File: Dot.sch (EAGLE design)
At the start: 42 parts, among them IC1 CAT24M010TS, IC2 SI1145, U1 ATMEGA328P-MU-QFN32, U2 TMP102, U3 ISL29125, U4 9DoF IMU, U5 BMP18

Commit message: Add chrystal oscillator, moved C2 and C3
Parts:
- added Y1: (no value), SparkFun-Clocks:RESONATORSMD-3.2X1.3
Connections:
- new net N$6: U1.PB6(XTAL1/TOSC1/PCINT6), Y1.3
- new net N$8: U1.PB7(XTAL2/TOSC2/PCINT7), Y1.1
- net GND: now also Y1.2
- net INT_MULTIPLE: now also U1.PB2(SS/OC1B/PCINT2); no longer U1.PB7(XTAL2/TOSC2/PCINT7)
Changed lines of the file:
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@@
 <part name="C7" library="resistor" deviceset="C-EU" device="C0603" value="0.1uF"/>
 <part name="SJ6" library="SparkFun" deviceset="SOLDERJUMPER" device="NC2"/>
+<part name="Y1" library="SparkFun-Clocks" deviceset="RESONATOR" device="SMD-3.2X1.3"/>
+<part name="SUPPLY30" library="supply2" deviceset="GND" device=""/>
 </parts>
 <sheets>
@@
 <instance part="C7" gate="G$1" x="66.04" y="129.54" rot="R90"/>
 <instance part="SJ6" gate="1" x="-43.18" y="147.32" rot="R90"/>
+<instance part="Y1" gate="G$1" x="200.66" y="66.04" rot="R90"/>
+<instance part="SUPPLY30" gate="GND" x="208.28" y="63.5"/>
 </instances>
 <busses>
@@
 <pinref part="R1" gate="G$1" pin="1"/>
 <pinref part="SUPPLY16" gate="GND" pin="GND"/>
+</segment>
+<segment>
+<pinref part="Y1" gate="G$1" pin="2"/>
+<pinref part="SUPPLY30" gate="GND" pin="GND"/>
 </segment>
 </net>
@@
 </segment>
 <segment>
-<pinref part="U1" gate="G$1" pin="PB7(XTAL2/TOSC2/PCINT7)"/>
-<wire x1="195.58" y1="63.5" x2="198.12" y2="63.5" width="0.1524" layer="91"/>
-<label x="198.12" y="63.5" size="1.27" layer="95" xref="yes"/>
-</segment>
-<segment>
 <pinref part="U2" gate="G$1" pin="ALERT"/>
 <wire x1="185.42" y1="-15.24" x2="187.96" y2="-15.24" width="0.1524" layer="91"/>
@@
 <label x="370.84" y="-30.48" size="1.27" layer="95" xref="yes"/>
 </segment>
-</net>
+<segment>
+<pinref part="U1" gate="G$1" pin="PB2(SS/OC1B/PCINT2)"/>
+<wire x1="195.58" y1="81.28" x2="198.12" y2="81.28" width="0.1524" layer="91"/>
+<label x="198.12" y="81.28" size="1.27" layer="95" xref="yes"/>
+</segment>
+</net>
+<net name="N$6" class="0">
+<segment>
+<pinref part="U1" gate="G$1" pin="PB6(XTAL1/TOSC1/PCINT6)"/>
+<pinref part="Y1" gate="G$1" pin="3"/>
+<wire x1="200.66" y1="68.58" x2="195.58" y2="68.58" width="0.1524" layer="91"/>
+</segment>
+</net>
+<net name="N$8" class="0">
+<segment>
+<pinref part="U1" gate="G$1" pin="PB7(XTAL2/TOSC2/PCINT7)"/>
+<pinref part="Y1" gate="G$1" pin="1"/>
+<wire x1="200.66" y1="63.5" x2="195.58" y2="63.5" width="0.1524" layer="91"/>
+</segment>
+</net>

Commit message: Add C10 1000uF with enough room, move HexID to other side
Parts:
- removed SJ1: SOLDERJUMPERNO, SparkFun:SOLDERJUMPERNO
- added C10: 1500uF 4V, adafruit:CPOL-USCT7343
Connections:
- removed net N$2: IC1.A1, SJ1.1
- net +3V3: now also C10.+; no longer SJ1.2
- net GND: now also C10.-
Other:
- note added: "Use https://goo.gl/ZxW9QR"
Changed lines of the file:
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@@
 <setting verticaltext="up"/>
 </settings>
-<grid distance="0.1" unitdist="inch" unit="inch" style="lines" multiple="1" display="no" altdistance="0.01" altunitdist="inch" altunit="inch"/>
+<grid distance="0.127" unitdist="mm" unit="mm" style="lines" multiple="1" display="no" altdistance="0.01" altunitdist="inch" altunit="inch"/>
 <layers>
 <layer number="1" name="Top" color="4" fill="1" visible="no" active="no"/>
@@
 <part name="+3V6" library="supply1" deviceset="+3V3" device=""/>
 <part name="+3V7" library="supply1" deviceset="+3V3" device=""/>
-<part name="+3V1" library="supply1" deviceset="+3V3" device=""/>
 <part name="JP2" library="pinhead" deviceset="PINHD-1X4" device=""/>
 <part name="LOGO1" library="Particle-Devices" deviceset="OSHW-LOGO" device="S"/>
@@
 <part name="R4" library="resistor" deviceset="R-EU_" device="R0603"/>
 <part name="BAT1" library="Battery" deviceset="BATTERY" device="20PTH"/>
-<part name="SJ1" library="SparkFun" deviceset="SOLDERJUMPER" device="NO"/>
 <part name="SW1" library="Seeed-OPL-Switch" deviceset="SMD-BUTTON(2P-6.0X3.0X2.5MM)" device="-DHT-1163S"/>
 <part name="U2" library="SparkFun" deviceset="TMP102" device=""/>
@@
 <part name="Y1" library="SparkFun-Clocks" deviceset="RESONATOR" device="SMD-3.2X1.3"/>
 <part name="SUPPLY30" library="supply2" deviceset="GND" device=""/>
+<part name="C10" library="adafruit" deviceset="CPOL-US" device="CT7343" value="1500uF 4V"/>
 </parts>
 <sheets>
@@
 <text x="1.778" y="50.8" size="1.27" layer="91">Red</text>
 <text x="-60.96" y="134.62" size="1.778" layer="91">Voltage Divider Lower R</text>
+<text x="-16.129" y="176.022" size="0.8128" layer="91">Use https://goo.gl/ZxW9QR</text>
 </plain>
 <instances>
@@
 <instance part="+3V6" gate="G$1" x="66.04" y="195.58"/>
 <instance part="+3V7" gate="G$1" x="88.9" y="58.42"/>
-<instance part="+3V1" gate="G$1" x="45.72" y="53.34"/>
 <instance part="JP2" gate="A" x="76.2" y="180.34"/>
 <instance part="LOGO1" gate="G$1" x="177.8" y="175.26"/>
@@
 <instance part="R4" gate="G$1" x="66.04" y="157.48" rot="R90"/>
 <instance part="BAT1" gate="G$1" x="27.94" y="165.1" rot="R270"/>
-<instance part="SJ1" gate="1" x="50.8" y="40.64" rot="R180"/>
 <instance part="SW1" gate="G$1" x="274.32" y="127"/>
 <instance part="U2" gate="G$1" x="175.26" y="-12.7"/>
@@
 <instance part="Y1" gate="G$1" x="200.66" y="66.04" rot="R90"/>
 <instance part="SUPPLY30" gate="GND" x="208.28" y="63.5"/>
+<instance part="C10" gate="G$1" x="-16.51" y="163.83"/>
 </instances>
 <busses>
@@
 <wire x1="2.54" y1="158.75" x2="10.16" y2="158.75" width="0.1524" layer="91"/>
 <junction x="10.16" y="158.75"/>
+<pinref part="C10" gate="G$1" pin="-"/>
+<wire x1="-16.51" y1="158.75" x2="2.54" y2="158.75" width="0.1524" layer="91"/>
+<junction x="2.54" y="158.75"/>
 </segment>
 <segment>
@@
 <wire x1="0" y1="55.88" x2="0" y2="50.8" width="0.1524" layer="91"/>
 <label x="0" y="50.8" size="1.27" layer="95" rot="R270" xref="yes"/>
-</segment>
-</net>
-<net name="N$2" class="0">
-<segment>
-<pinref part="IC1" gate="G$1" pin="A1"/>
-<wire x1="55.88" y1="40.64" x2="58.42" y2="40.64" width="0.1524" layer="91"/>
-<pinref part="SJ1" gate="1" pin="1"/>
 </segment>
 </net>
@@
 </segment>
 <segment>
-<pinref part="+3V1" gate="G$1" pin="+3V3"/>
-<pinref part="SJ1" gate="1" pin="2"/>
-<wire x1="45.72" y1="50.8" x2="45.72" y2="40.64" width="0.1524" layer="91"/>
-</segment>
-<segment>
 <pinref part="SJ4" gate="G$1" pin="3"/>
 <pinref part="+3V12" gate="G$1" pin="+3V3"/>
@@
 <wire x1="2.54" y1="166.37" x2="10.16" y2="166.37" width="0.1524" layer="91"/>
 <junction x="10.16" y="166.37"/>
+<pinref part="C10" gate="G$1" pin="+"/>
+<wire x1="-16.51" y1="166.37" x2="2.54" y2="166.37" width="0.1524" layer="91"/>
+<junction x="2.54" y="166.37"/>
 </segment>
 </net>
@@
 </segment>
 </net>
+<net name="N$2" class="0">
+<segment>
+<wire x1="-16.51" y1="167.64" x2="-16.51" y2="168.91" width="0.1524" layer="91"/>
+<wire x1="-16.51" y1="168.91" x2="-8.89" y2="175.26" width="0.1524" layer="91"/>
+<wire x1="-16.51" y1="167.64" x2="-17.145" y2="168.275" width="0.1524" layer="91"/>
+<wire x1="-16.51" y1="167.64" x2="-15.875" y2="168.275" width="0.1524" layer="91"/>
+<wire x1="-8.89" y1="175.26" x2="-2.54" y2="175.26" width="0.1524" layer="91"/>
+</segment>
+</net>

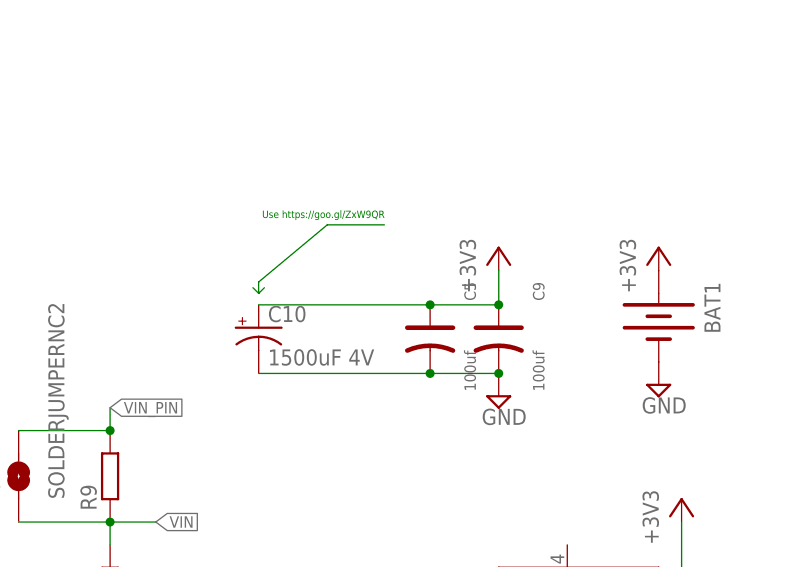
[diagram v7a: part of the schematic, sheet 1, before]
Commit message: Remove C9 100uF add Zenner 3.6V
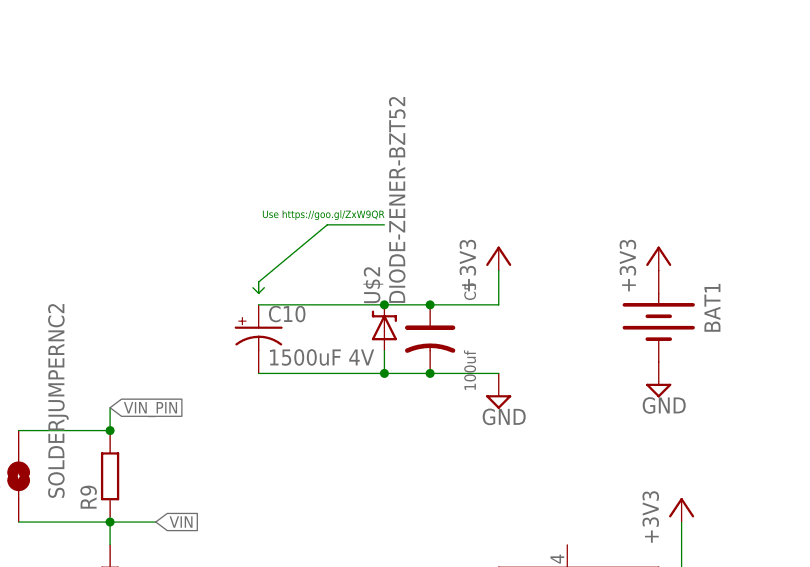
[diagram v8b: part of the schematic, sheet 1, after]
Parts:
- removed C9: 100uf, Seeed-OPL-Capacitor:TANTALUM-SMD-100UF-6.3V(AVX-A)
- added U$2: DIODE-ZENER-BZT52, SparkFun:DIODE-ZENER-BZT52
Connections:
- net +3V3: now also U$2.C; no longer C9.+
- net GND: now also U$2.A; no longer C9.-
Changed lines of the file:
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@@
 <setting verticaltext="up"/>
 </settings>
-<grid distance="0.127" unitdist="mm" unit="mm" style="lines" multiple="1" display="no" altdistance="0.01" altunitdist="inch" altunit="inch"/>
+<grid distance="1.27" unitdist="mm" unit="mm" style="lines" multiple="1" display="no" altdistance="0.01" altunitdist="inch" altunit="inch"/>
 <layers>
 <layer number="1" name="Top" color="4" fill="1" visible="no" active="no"/>
@@
 <part name="LED1" library="led" deviceset="GM1WA55311A" device=""/>
 <part name="SUPPLY28" library="supply2" deviceset="GND" device=""/>
-<part name="C9" library="Seeed-OPL-Capacitor" deviceset="TANTALUM-SMD-100UF-6.3V(AVX-A)" device="" value="100uf"/>
 <part name="+3V20" library="supply1" deviceset="+3V3" device=""/>
 <part name="SUPPLY29" library="supply2" deviceset="GND" device=""/>
@@
 <part name="SUPPLY30" library="supply2" deviceset="GND" device=""/>
 <part name="C10" library="adafruit" deviceset="CPOL-US" device="CT7343" value="1500uF 4V"/>
+<part name="U$2" library="SparkFun" deviceset="DIODE-ZENER" device="-BZT52"/>
 </parts>
 <sheets>
@@
 <instance part="LED1" gate="G$1" x="-10.16" y="73.66"/>
 <instance part="SUPPLY28" gate="GND" x="45.72" y="-35.56"/>
-<instance part="C9" gate="G$1" x="10.16" y="162.56" rot="R270"/>
 <instance part="+3V20" gate="G$1" x="10.16" y="172.72"/>
 <instance part="SUPPLY29" gate="GND" x="10.16" y="156.21"/>
@@
 <instance part="SUPPLY30" gate="GND" x="208.28" y="63.5"/>
 <instance part="C10" gate="G$1" x="-16.51" y="163.83"/>
+<instance part="U$2" gate="G$1" x="-2.54" y="163.83" rot="R90"/>
 </instances>
 <busses>
@@
 </segment>
 <segment>
-<pinref part="C9" gate="G$1" pin="-"/>
 <pinref part="SUPPLY29" gate="GND" pin="GND"/>
 <pinref part="C5" gate="G$1" pin="-"/>
 <wire x1="2.54" y1="158.75" x2="10.16" y2="158.75" width="0.1524" layer="91"/>
-<junction x="10.16" y="158.75"/>
 <pinref part="C10" gate="G$1" pin="-"/>
-<wire x1="-16.51" y1="158.75" x2="2.54" y2="158.75" width="0.1524" layer="91"/>
+<wire x1="-16.51" y1="158.75" x2="-2.54" y2="158.75" width="0.1524" layer="91"/>
 <junction x="2.54" y="158.75"/>
+<pinref part="U$2" gate="G$1" pin="A"/>
+<wire x1="-2.54" y1="158.75" x2="2.54" y2="158.75" width="0.1524" layer="91"/>
+<wire x1="-2.54" y1="161.29" x2="-2.54" y2="158.75" width="0.1524" layer="91"/>
+<junction x="-2.54" y="158.75"/>
 </segment>
 <segment>
@@
 <segment>
 <pinref part="+3V20" gate="G$1" pin="+3V3"/>
-<pinref part="C9" gate="G$1" pin="+"/>
 <wire x1="10.16" y1="170.18" x2="10.16" y2="166.37" width="0.1524" layer="91"/>
 <pinref part="C5" gate="G$1" pin="+"/>
 <wire x1="2.54" y1="166.37" x2="10.16" y2="166.37" width="0.1524" layer="91"/>
-<junction x="10.16" y="166.37"/>
 <pinref part="C10" gate="G$1" pin="+"/>
-<wire x1="-16.51" y1="166.37" x2="2.54" y2="166.37" width="0.1524" layer="91"/>
+<wire x1="-16.51" y1="166.37" x2="-2.54" y2="166.37" width="0.1524" layer="91"/>
 <junction x="2.54" y="166.37"/>
-</segment>
-</net>
+<pinref part="U$2" gate="G$1" pin="C"/>
+<wire x1="-2.54" y1="166.37" x2="2.54" y2="166.37" width="0.1524" layer="91"/>
+<junction x="-2.54" y="166.37"/>
+</segment>
+</net>
